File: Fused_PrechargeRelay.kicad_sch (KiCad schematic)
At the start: 14 parts, among them K2 DE1a-12V, Q4 2N7002

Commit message: saving
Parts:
- removed Q4: 2N7002, Package_TO_SOT_SMD:SOT-23, symbol Transistor_FET:2N7002
- added Q?: NMOS, ActivePrecharge-RevB:RES_PWR263S-35-3300F, symbol Simulation_SPICE:NMOS
- added R? (x2): R, symbol Device:R
- added U5: EL3H7, LHRS_ICs:EL3H7, symbol lhrs_ics:EL3H7
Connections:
- net DRAIN: now also Q?.1 (D)
- net GND: now also U5.2
- net HVGND: now also R?.1
- net PRECHARGE_CTRL: now also R?.1
- new net: R?.2, U5.1
- new net HVPRECHARGE_CTRL: R?.2, U5.3
- new net ISO_5V: U5.4
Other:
- note added: "S = GND"
- note added: "in from mcu + lil R"
- note added: "optic is isolation for precharge control"
- moved on the sheet: D12, F8, K2, R35, R36

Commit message: final schematic REV-A?
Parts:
- removed F8: 0.5A, symbol Device:Fuse
- removed R35: 10k, Package_DIP:DIP-8_W7.62mm, symbol Device:R
- removed R36: 1k, Package_DIP:DIP-8_W7.62mm, symbol Device:R
- removed R? (x2): R, symbol Device:R
- removed U5: EL3H7, LHRS_ICs:EL3H7, symbol lhrs_ics:EL3H7
- added R2, R3, R4, R5: 330, ActivePrecharge-RevB:RES_PWR263S-35-3300F, symbol Precharge-R:PWR263S-35-3300F
- gave numbers to parts that had none: 1
- renumbered D9 to D1, D10 to D2, D11 to D3, D12 to D4, F6 to F2, F7 to F3, K2 to K1, TP20 to TP1, TP21 to TP2, TP22 to TP3
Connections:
- net VPRE_OUT is gone; now on net HV-: K1.4 (N.O.)
- net HV+: now also R2.2, R3.2, R4.2, R5.2
- net HVGND: now also Q1.3 (S)
- net HV_PRECHARGE_CTRL: now reaches Q1.2 (G)
- net RES_HV-: now reaches K1.3 (COM)
- net RES_HV-: now also R2.1, R3.1, R4.1, R5.1
- new net RESISTORS: R2.3, R3.3, R4.3, R5.3
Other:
- note added: "Precharge Circuit Parameters: Battery Vmax: 135V Target Time (Tmax): 0.25 s Precharge Level: 95% System Capacitance (C): 1420µF Resistor Selection (R): 50 ohms Fuse Logic : Peak Inrush Current: 2.7A Margin: 3A fuse too close to 2.7A peak Selected: 5A"
- note added: "Precharge Resistors"
- note removed: "Fuse Logic : Peak Inrush Current: 0.0166A DE1a-12V relay coil draws 16.6 mA (0.0166 A) Margin: 3A fuse too close to 2.7A peak Selected: 0.5A"
- note removed: "Precharge Circuit Parameters : Battery Vmax: 135V Target Time (Tmax): 0.25 s Precharge Level: 95% System Capacitance (C): 1420µF Resistor Selection (R): 50 ohms Fuse Logic : Peak Inrush Current: 2.7A Margin: 3A fuse too close to 2.7A peak Selected: 5A"
- note removed: "S = GND"
- note removed: "in from mcu + lil R"
- note removed: "optic is isolation for precharge control"
- moved on the sheet: D1, D2, D3, D4, F2, F3, K1, Q1, TP1, TP2, TP3

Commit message: main isolation & motor isolation
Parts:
- K1: footprint DE1a12V -> LIB_DE1a-12V:DE1a12V
- R2, R3, R4, R5: value 330 -> 50; footprint ActivePrecharge-RevB:RES_PWR263S-35-3300F -> PWR263S-35-3300F:RES_PWR263S-35-3300F
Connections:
- net RESISTORS renamed RESISTOR
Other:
- note added: "Resistor (R) = 50 ohms : Battery Vmax: 135V Target Time (Tmax): 0.25 s Precharge Level: 95% System Capacitance (C): 1420µF Fuse = 5A : Peak Inrush Current: 2.7A 3A fuse too close to 2.7A peak"
- note removed: "Precharge Circuit Parameters: Battery Vmax: 135V Target Time (Tmax): 0.25 s Precharge Level: 95% System Capacitance (C): 1420µF Resistor Selection (R): 50 ohms Fuse Logic : Peak Inrush Current: 2.7A Margin: 3A fuse too close to 2.7A peak Selected: 5A"
- moved on the sheet: K1, Q1

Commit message: removed isolation for AMC3311
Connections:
- net HVGND: no longer Q1.3 (S)
- new net GND: Q1.3 (S)
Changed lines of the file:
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@@
 		)
 	)
-	(hierarchical_label "HVGND"
+	(hierarchical_label "GND"
 		(shape output)
 		(at 210.82 45.72 0)

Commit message: seperated hv+ and hv- for main and motor
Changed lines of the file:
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@@
+		)
+	)
+	(polyline
+		(pts
+			(xy 179.07 26.67) (xy 179.07 36.83)
+		)
+		(stroke
+			(width 0)
+			(type dash)
 		)
 	)

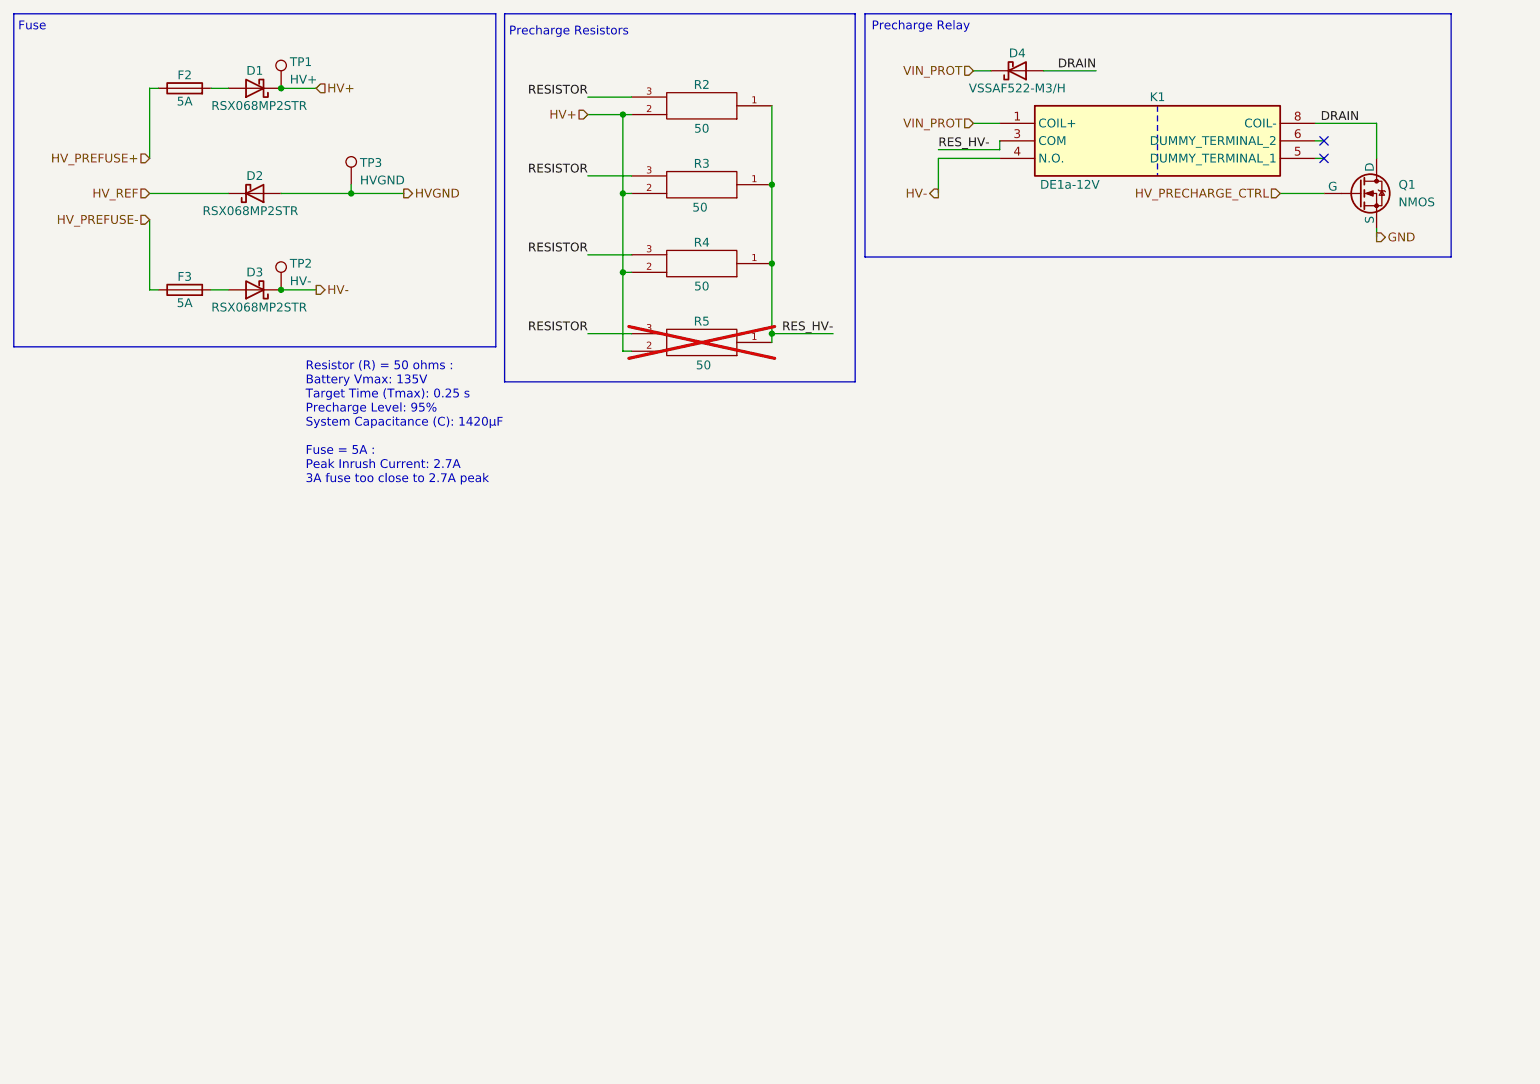
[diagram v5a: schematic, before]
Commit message: added testpoints
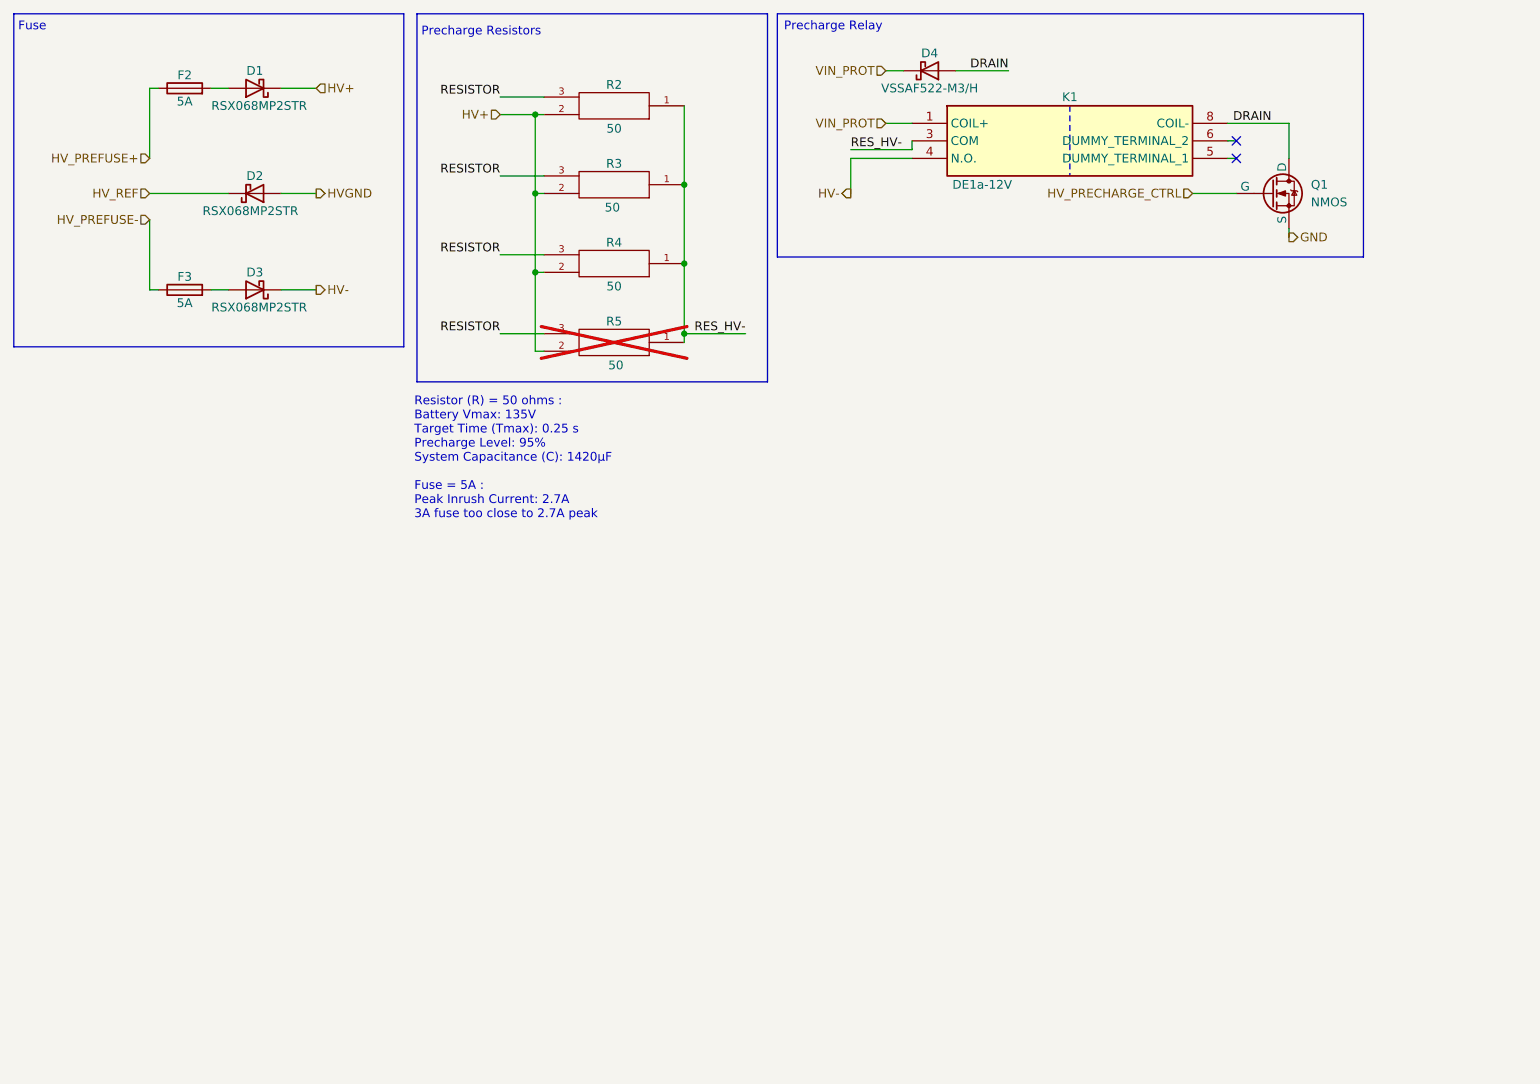
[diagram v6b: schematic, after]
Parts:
- removed TP1: HV+, TestPoint:TestPoint_Loop_D1.80mm_Drill1.0mm_Beaded, symbol lhrs_misc:Multimeter_TP
- removed TP2: HV-, TestPoint:TestPoint_Loop_D1.80mm_Drill1.0mm_Beaded, symbol lhrs_misc:Multimeter_TP
- removed TP3: HVGND, TestPoint:TestPoint_Loop_D1.80mm_Drill1.0mm_Beaded, symbol lhrs_misc:Multimeter_TP
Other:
- moved on the sheet: D4, K1, Q1, R2, R3, R4, R5

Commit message: AGND
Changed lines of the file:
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@@
 	(text "Resistor (R) = 50 ohms :\nBattery Vmax: 135V\nTarget Time (Tmax): 0.25 s\nPrecharge Level: 95%\nSystem Capacitance (C): 1420µF\n\nFuse = 5A :\nPeak Inrush Current: 2.7A\n3A fuse too close to 2.7A peak"
 		(exclude_from_sim no)
-		(at 71.374 68.834 0)
+		(at 71.12 68.58 0)
 		(effects
 			(font
@@
 	)
 	(hierarchical_label "GND"
-		(shape output)
+		(shape bidirectional)
 		(at 198.12 45.72 0)
 		(effects
@@
 			(project "PS-PrechargeBoard"
 				(path "/74d17fe6-68d4-4bd7-954a-e2bbb58b1f1e/90c6c4b7-1465-4e8f-80ba-ec6b0750446b"
-					(reference "R26")
+					(reference "R46")
 					(unit 1)
 				)
@@
 			(project "PS-PrechargeBoard"
 				(path "/74d17fe6-68d4-4bd7-954a-e2bbb58b1f1e/90c6c4b7-1465-4e8f-80ba-ec6b0750446b"
-					(reference "R29")
+					(reference "R49")
 					(unit 1)
 				)
@@
 			(project "PS-PrechargeBoard"
 				(path "/74d17fe6-68d4-4bd7-954a-e2bbb58b1f1e/90c6c4b7-1465-4e8f-80ba-ec6b0750446b"
-					(reference "R28")
+					(reference "R48")
 					(unit 1)
 				)
@@
 			(project "PS-PrechargeBoard"
 				(path "/74d17fe6-68d4-4bd7-954a-e2bbb58b1f1e/90c6c4b7-1465-4e8f-80ba-ec6b0750446b"
-					(reference "R27")
+					(reference "R47")
 					(unit 1)
 				)

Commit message: isolated precharge from fuse
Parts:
- removed D4: VSSAF522-M3/H, UTSVT-Passives:SODFL5026X125N, symbol Device:D_Schottky
- removed K1: DE1a-12V, LIB_DE1a-12V:DE1a12V, symbol DE1a-12V:DE1a-12V
- removed Q1: NMOS, ActivePrecharge-RevB:RES_PWR263S-35-3300F, symbol Simulation_SPICE:NMOS
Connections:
- no-connect marks 2 -> 0
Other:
- note removed: "Precharge Relay"
